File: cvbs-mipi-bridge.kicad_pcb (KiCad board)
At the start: 4 copper layers, 55 x 70 mm, 107 parts, among them IC1 ADV7280BCPZ-M, IC2 TLV70018, IC4 SN74AUP1G17DCKR, IC5 SN74AUP1G17DCKR, J1 WE_68715014522, J2 1053131102, J3 KLPX-0848A-2-Y, J4 KLPX-0848A-2-Y, J5 KLPX-0848A-2-Y, J6 KLPX-0848A-2-Y, J7 61300211121, Q1 BSS138APW, Q2 BSS138APW, Q3 BSS138APW, Q4 BSS138APW, Y1 ABM8G-28.63636MHZ-18-D2Y-T

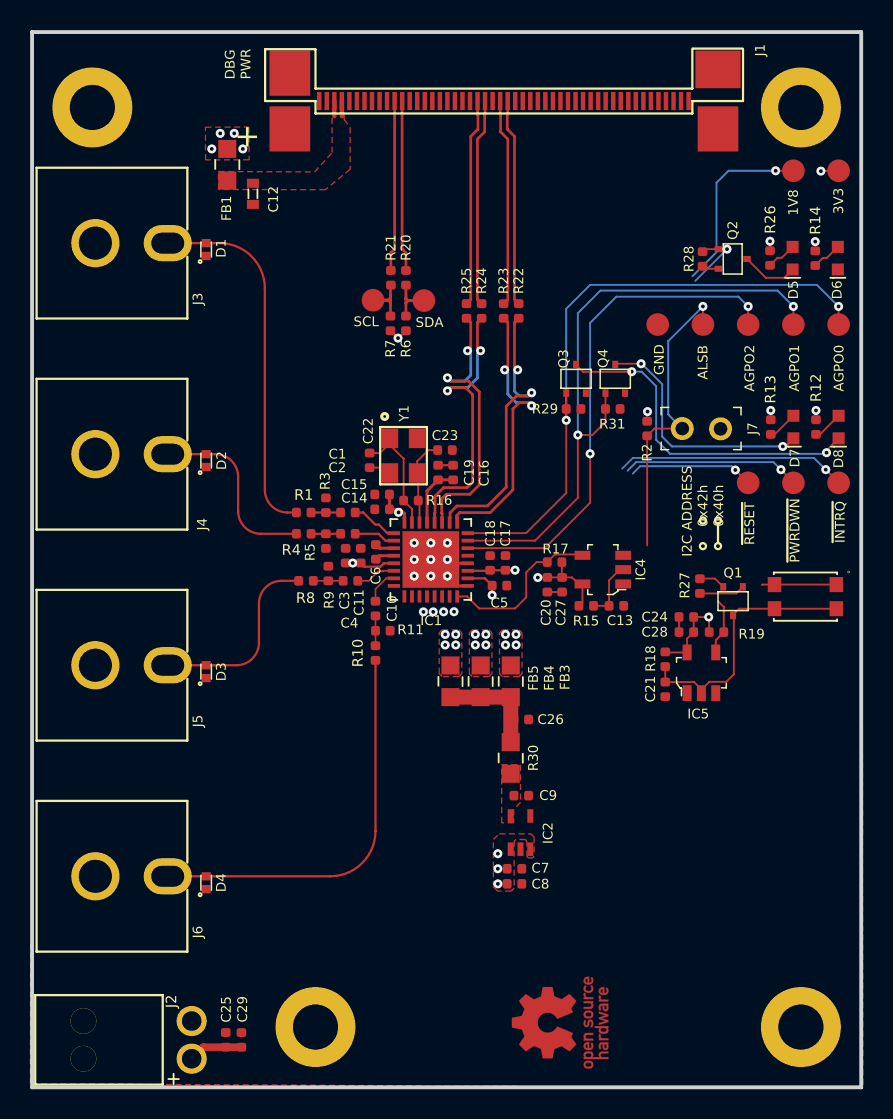
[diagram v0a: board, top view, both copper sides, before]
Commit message: Routed auxiliary signals
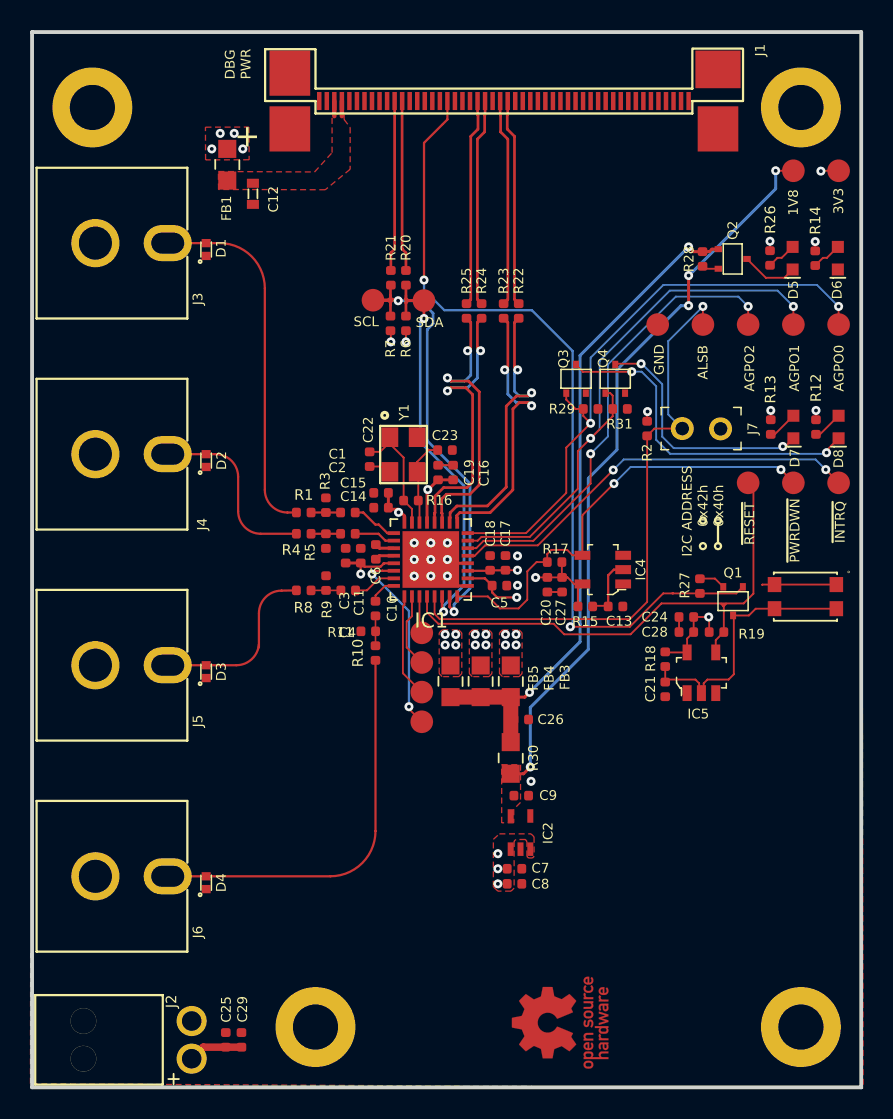
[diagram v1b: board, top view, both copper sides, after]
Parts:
- added TP14: TP, cvbs-mipi-bridge-footprints:TP-R-1.5, F.Cu at (137.6, 99.8)
- added TP15: TP, cvbs-mipi-bridge-footprints:TP-R-1.5, F.Cu at (137.6, 97.8)
- added TP16: TP, cvbs-mipi-bridge-footprints:TP-R-1.5, F.Cu at (137.6, 95.8)
- added TP4: TP, cvbs-mipi-bridge-footprints:TP-R-1.5, F.Cu at (137.6, 101.8)
- IC1: value ADV7280BCPZ-M -> ADV7282-M; footprint cvbs-mipi-bridge-footprints:LFCSP-32-1EP-5x5mm -> antmicro-footprints:LFCSP-32-1EP-5x5mm
- moved R29 1.13 mm to (148.8, 81.0)
- moved R11 0.97 mm to (134.0, 95.8), turned to 0 degrees
- moved C4 0.65 mm to (132.7, 93.0)
- moved R8 0.65 mm to (129.7, 93.0)
- moved R9 0.65 mm to (131.2, 92.5)
- moved R31 0.48 mm to (150.7, 81.0)
- moved C14 0.13 mm to (134.8, 87.5)
- moved C15 0.13 mm to (134.9, 86.6)
- moved C22 0.08 mm to (134.1, 84.3)
- moved Y1 0.08 mm to (136.4, 84.0)
- moved C13 0.07 mm to (150.4, 94.1)
- moved R15 0.07 mm to (148.4, 94.1)
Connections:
- IC1 pad 22: /AIN3 -> Net-(IC1-Pad22)
- IC1 pad 23: /AIN4 -> /AIN3
- IC1 pad 24: unconnected-(IC1-Pad24) -> /AIN4
- IC1 pad 25: unconnected-(IC1-Pad25) -> Net-(IC1-Pad25)
- IC1 pad 26: unconnected-(IC1-Pad26) -> Net-(IC1-Pad26)
- IC1 pad 27: unconnected-(IC1-Pad27) -> Net-(IC1-Pad27)
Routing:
- net /RST_IN: track 3.03 -> 55.7 mm, vias 0 -> 2
- net Net-(C9-Pad1): track 12.3 -> 49.3 mm, vias 1 -> 4
- net 1V8_SYS: track 11.4 -> 44.5 mm, vias 1 -> 2
- net /SCL: track 6.01 -> 32.3 mm, vias 1 -> 2
- net /RESET: track 12.1 -> 35.8 mm, vias 2 -> 0
- net /SDA: track 5.10 -> 28.7 mm, vias 1 -> 2
- net /ALSB: track 20.4 -> 40.1 mm, vias 2 -> 1
- net Net-(IC1-Pad22): track 0.00 -> 12.7 mm, vias 0 -> 2
- net Net-(IC1-Pad5): track 15.3 -> 27.9 mm, vias 1 -> 2
- net DVDD_1V8: track 11.7 -> 23.5 mm, vias 5 -> 6
- net /PWRDWN: track 22.8 -> 30.2 mm, vias 1 -> 2
- net Net-(IC1-Pad25): track 0.00 -> 6.90 mm
- net Net-(IC1-Pad26): track 0.00 -> 4.94 mm
- net /AGPO1: track 41.4 -> 38.2 mm
- net Net-(IC1-Pad6): track 34.3 -> 31.3 mm
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
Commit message: Connected GNDs, cleaned DRC
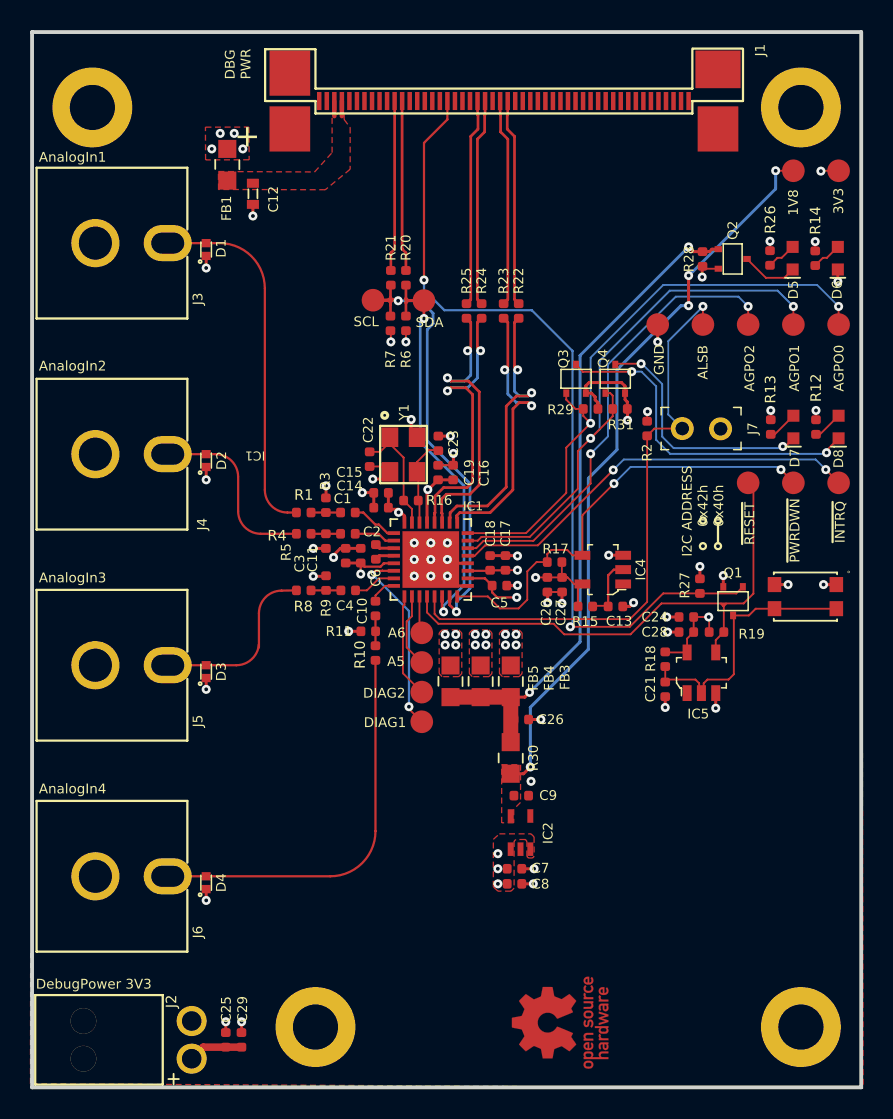
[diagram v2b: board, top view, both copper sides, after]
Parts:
- moved C23 0.62 mm to (138.7, 83.3), turned to 90 degrees
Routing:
- net GND: track 15.0 -> 47.3 mm, vias 12 -> 48
- net Net-(C21-Pad1): track 18.8 -> 18.2 mm
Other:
- board text added: "A5"
- board text added: "A6"
- board text added: "AnalogIn1"
- board text added: "AnalogIn2"
- board text added: "AnalogIn3"
- board text added: "AnalogIn4"
- board text added: "DIAG1"
- board text added: "DIAG2"
- board text added: "DebugPower 3V3"
- board text added: "IC1"

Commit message: Updated zones
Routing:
- added copper zone on B.Cu, net GND
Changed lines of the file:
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@@
   (segment (start 144.627466 80.137464) (end 144.836465 79.928465) (width 0.182) (layer "B.Cu") (net 29))
   (segment (start 144.010009 80.137465) (end 144.627466 80.137464) (width 0.182) (layer "B.Cu") (net 29))
-  (segment (start 141.36416 86.036095) (end 141.36416 79.861618) (width 0.182) (layer "F.Cu") (net 30))
+  (segment (start 140.651542 79.149) (end 139.463364 79.148999) (width 0.182) (layer "F.Cu") (net 30))
+  (segment (start 138.87051 87.896888) (end 138.87051 87.2) (width 0.182) (layer "F.Cu") (net 30))
   (segment (start 140.798999 76.928972) (end 140.59 77.137971) (width 0.182) (layer "F.Cu") (net 30))
-  (segment (start 139.18056 86.658582) (end 140.741673 86.658582) (width 0.182) (layer "F.Cu") (net 30))
   (segment (start 140.798999 75.263999) (end 140.798999 76.928972) (width 0.182) (layer "F.Cu") (net 30))
+  (segment (start 138.87051 87.2) (end 139.18056 86.88995) (width 0.182) (layer "F.Cu") (net 30))
+  (segment (start 138.899511 87.925889) (end 138.87051 87.896888) (width 0.182) (layer "F.Cu") (net 30))
   (segment (start 141.36416 79.861618) (end 140.651542 79.149) (width 0.182) (layer "F.Cu") (net 30))
-  (segment (start 138.899511 87.925889) (end 138.87051 87.896888) (width 0.182) (layer "F.Cu") (net 30))
-  (segment (start 138.87051 87.896888) (end 138.87051 86.968632) (width 0.182) (layer "F.Cu") (net 30))
+  (segment (start 140.741673 86.88995) (end 141.36416 86.267463) (width 0.182) (layer "F.Cu") (net 30))
+  (segment (start 140.52 74.985) (end 140.798999 75.263999) (width 0.182) (layer "F.Cu") (net 30))
   (segment (start 139.463364 79.148999) (end 139.254365 78.94) (width 0.182) (layer "F.Cu") (net 30))
-  (segment (start 138.87051 86.968632) (end 139.18056 86.658582) (width 0.182) (layer "F.Cu") (net 30))
-  (segment (start 140.52 74.985) (end 140.798999 75.263999) (width 0.182) (layer "F.Cu") (net 30))
-  (segment (start 140.651542 79.149) (end 139.463364 79.148999) (width 0.182) (layer "F.Cu") (net 30))
-  (segment (start 140.741673 86.658582) (end 141.36416 86.036095) (width 0.182) (layer "F.Cu") (net 30))
+  (segment (start 141.36416 86.267463) (end 141.36416 79.861618) (width 0.182) (layer "F.Cu") (net 30))
+  (segment (start 139.18056 86.88995) (end 140.741673 86.88995) (width 0.182) (layer "F.Cu") (net 30))
   (segment (start 138.899511 88.53549) (end 138.899511 87.925889) (width 0.182) (layer "F.Cu") (net 30))
   (via (at 139.254365 78.94) (size 0.6) (drill 0.25) (layers "F.Cu" "B.Cu") (net 30))
@@
   (segment (start 139.463364 79.148999) (end 140.408459 79.148999) (width 0.182) (layer "B.Cu") (net 30))
   (segment (start 140.408459 79.148999) (end 140.798999 78.758459) (width 0.182) (layer "B.Cu") (net 30))
-  (segment (start 138.428511 87.896888) (end 138.42851 86.785548) (width 0.182) (layer "F.Cu") (net 31))
-  (segment (start 140.92216 85.853011) (end 140.92216 80.044702) (width 0.182) (layer "F.Cu") (net 31))
+  (segment (start 138.42851 87.016916) (end 138.997476 86.44795) (width 0.182) (layer "F.Cu") (net 31))
+  (segment (start 140.92216 80.044702) (end 140.468458 79.591) (width 0.182) (layer "F.Cu") (net 31))
   (segment (start 141.241001 76.928972) (end 141.45 77.137971) (width 0.182) (layer "F.Cu") (net 31))
-  (segment (start 138.997476 86.216582) (end 140.558589 86.216582) (width 0.182) (layer "F.Cu") (net 31))
   (segment (start 138.39951 87.925889) (end 138.428511 87.896888) (width 0.182) (layer "F.Cu") (net 31))
-  (segment (start 140.558589 86.216582) (end 140.92216 85.853011) (width 0.182) (layer "F.Cu") (net 31))
+  (segment (start 140.468458 79.591) (end 139.463364 79.591001) (width 0.182) (layer "F.Cu") (net 31))
   (segment (start 139.463364 79.591001) (end 139.254365 79.8) (width 0.182) (layer "F.Cu") (net 31))
-  (segment (start 140.468458 79.591) (end 139.463364 79.591001) (width 0.182) (layer "F.Cu") (net 31))
-  (segment (start 140.92216 80.044702) (end 140.468458 79.591) (width 0.182) (layer "F.Cu") (net 31))
-  (segment (start 138.42851 86.785548) (end 138.997476 86.216582) (width 0.182) (layer "F.Cu") (net 31))
+  (segment (start 140.92216 86.084379) (end 140.92216 80.044702) (width 0.182) (layer "F.Cu") (net 31))
+  (segment (start 138.428511 87.896888) (end 138.42851 87.016916) (width 0.182) (layer "F.Cu") (net 31))
+  (segment (start 140.558589 86.44795) (end 140.92216 86.084379) (width 0.182) (layer "F.Cu") (net 31))
+  (segment (start 138.997476 86.44795) (end 140.558589 86.44795) (width 0.182) (layer "F.Cu") (net 31))
   (segment (start 141.241001 75.263999) (end 141.241001 76.928972) (width 0.182) (layer "F.Cu") (net 31))
   (segment (start 141.52 74.985) (end 141.241001 75.263999) (width 0.182) (layer "F.Cu") (net 31))
@@
     )
   )
+  (zone (net 0) (net_name "") (layer "F.Cu") (hatch edge 0.508)
+    (connect_pads (clearance 0))
+    (min_thickness 0.254)
+    (keepout (tracks allowed) (vias allowed) (pads allowed) (copperpour not_allowed) (footprints allowed))
+    (fill (thermal_gap 0.508) (thermal_bridge_width 0.508))
+    (polygon
+      (pts
+        (xy 144.4 62)
+        (xy 145.05 62.6)
+        (xy 145.95 63.4)
+        (xy 145.95 85.6)
+        (xy 142.25 89.45)
+        (xy 138.5 89.6)
+        (xy 138.5 85.95)
+        (xy 140 84.3)
+        (xy 140 82.4)
+        (xy 138.25 80.65)
+        (xy 138.25 63.85)
+        (xy 138.2 62.9)
+        (xy 140.1 60.75)
+        (xy 140.1 60)
+        (xy 144.4 60)
+      )
+    )
+  )
   (zone (net 12) (net_name "3V3_SYS") (layer "F.Cu") (hatch edge 0.508)
     (priority 1)
@@
       )
     )
+  )
+  (zone (net 0) (net_name "") (layer "B.Cu") (hatch edge 0.508)
+    (connect_pads (clearance 0))
+    (min_thickness 0.254)
+    (keepout (tracks allowed) (vias allowed) (pads allowed) (copperpour not_allowed) (footprints allowed))
+    (fill (thermal_gap 0.508) (thermal_bridge_width 0.508))
+    (polygon
+      (pts
+        (xy 147.55 77.2)
+        (xy 147.55 82.45)
+        (xy 145.076016 82.489738)
+        (xy 140.3 82.45)
+        (xy 138.266372 80.640205)
+        (xy 138.25 76.2)
+        (xy 138.25 74.45)
+        (xy 140.4 74.45)
+        (xy 144.85 74.45)
+      )
+    )
+  )
+  (zone (net 3) (net_name "GND") (layer "B.Cu") (hatch edge 0.508)
+    (connect_pads (clearance 0.2))
+    (min_thickness 0.254) (filled_areas_thickness no)
+    (fill yes (thermal_gap 0.508) (thermal_bridge_width 0.508))
+    (polygon
+      (pts
+        (xy 166.7 56.05)
+        (xy 166.7 125.95)
+        (xy 111.7 126)
+        (xy 111.75 56)
+      )
+    )

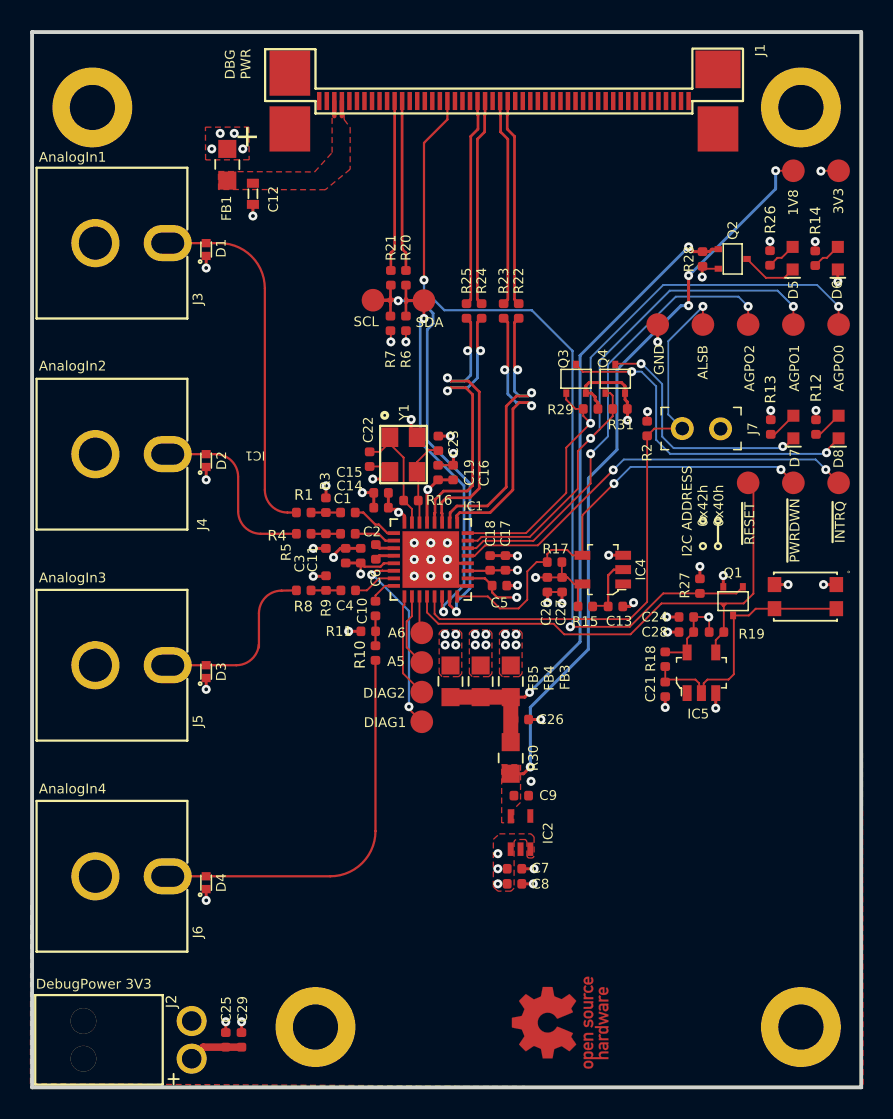
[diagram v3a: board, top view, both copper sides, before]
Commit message: Via stiching
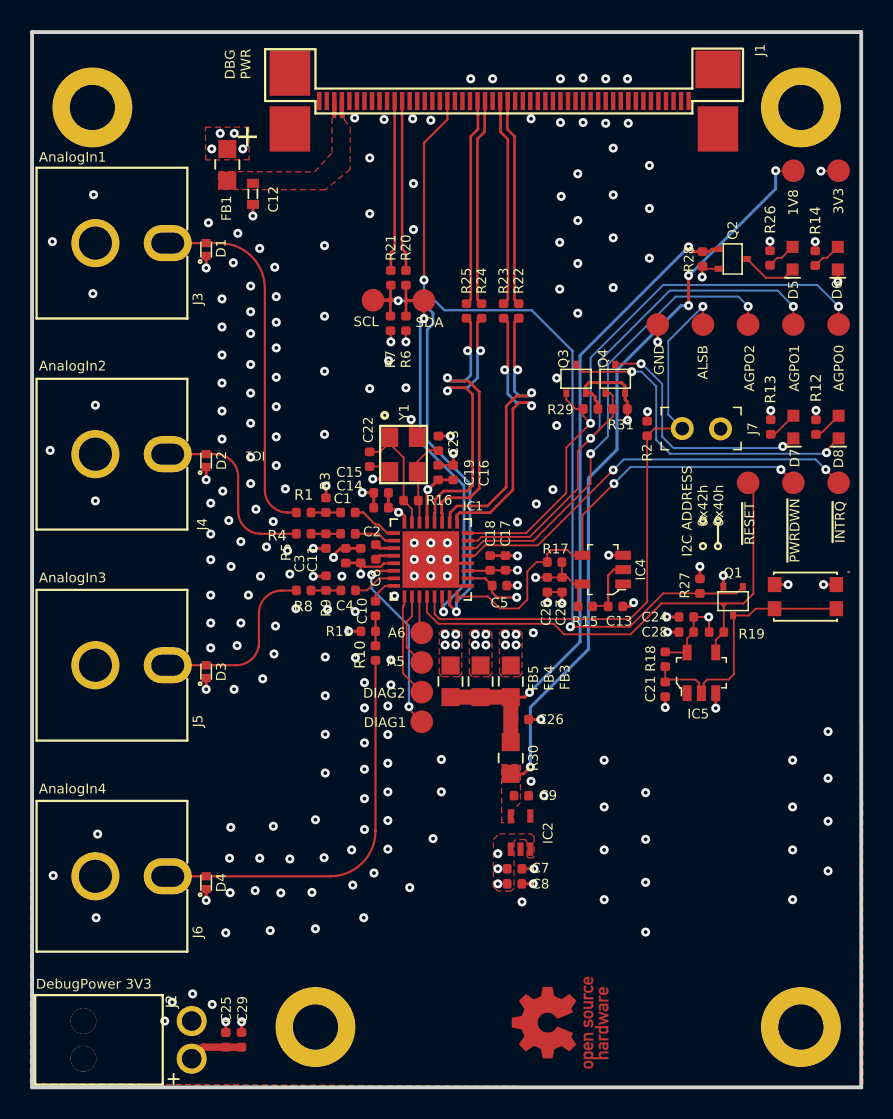
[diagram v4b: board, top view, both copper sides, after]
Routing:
- net GND: vias 48 -> 221

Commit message: Add coupling capacitors
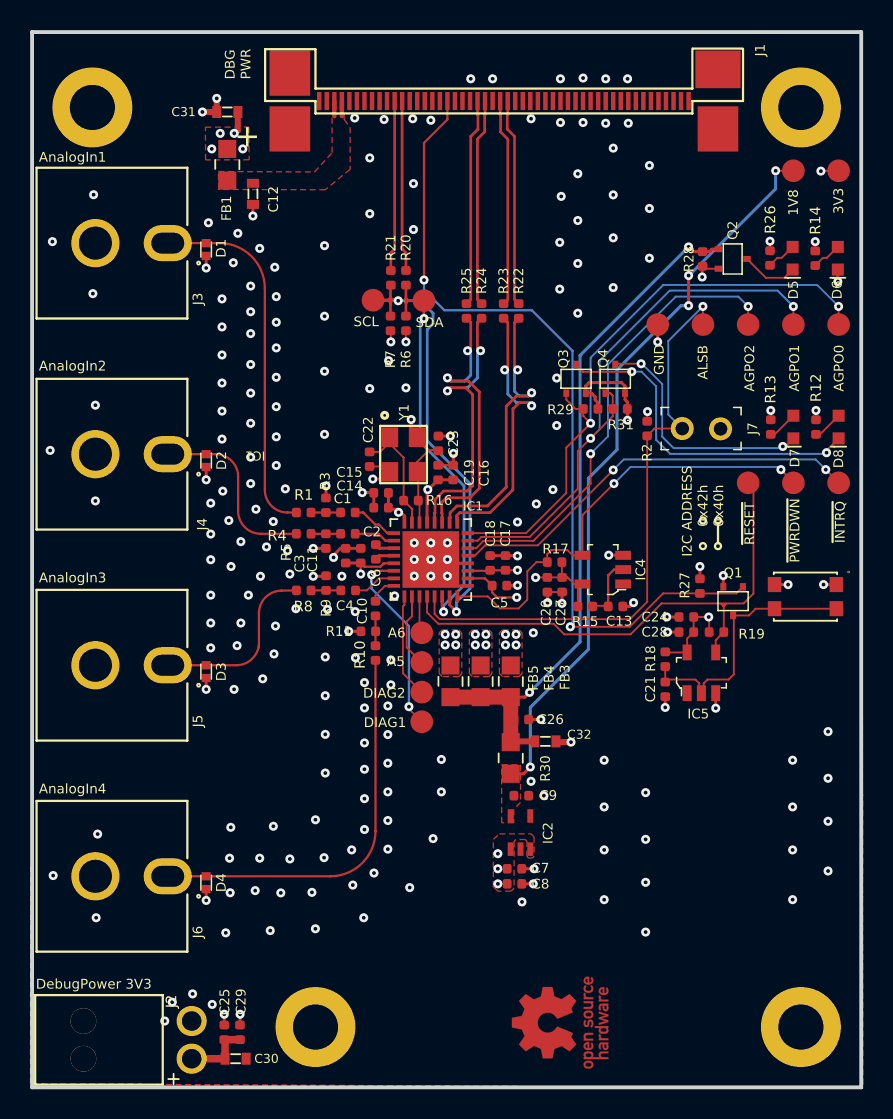
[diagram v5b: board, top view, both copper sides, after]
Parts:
- added C30: C_10u_0603, cvbs-mipi-bridge-footprints:0603-cap, F.Cu at (125.2, 124.1)
- added C31: C_10u_0603, cvbs-mipi-bridge-footprints:0603-cap, F.Cu at (124.7, 61.3)
- added C32: C_10u_0603, cvbs-mipi-bridge-footprints:0603-cap, F.Cu at (145.8, 103.0)
- IC1: footprint antmicro-footprints:LFCSP-32-1EP-5x5mm -> cvbs-mipi-bridge-footprints:LFCSP-32-1EP-5x5mm
- moved C29 0.51 mm to (125.5, 122.3)
- moved C25 0.51 mm to (124.5, 122.3)
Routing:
- net GND: track 47.3 -> 50.2 mm, vias 221 -> 224
- net 3V3_SYS: track 25.0 -> 27.2 mm
- net 1V8_SYS: track 44.5 -> 46.1 mm
